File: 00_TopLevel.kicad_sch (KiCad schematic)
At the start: 0 parts

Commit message: Further schematic structure
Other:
- added sheet 01_PowerInput (01_PowerInput.kicad_sch)
- added sheet 02_5VReg (02_5VReg.kicad_sch)
- added sheet 03_CoreReg (03_CoreReg.kicad_sch)
- added sheet 04_USB7206Core (04_USB7206Core.kicad_sch)
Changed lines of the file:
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@@
 	(generator_version "10.0")
 	(paper "A4")
+	(sheet
+		(at 88.9 25.4)
+		(size 38.1 25.4)
+		(exclude_from_sim no)
+		(in_bom yes)
+		(on_board yes)
+		(dnp no)
+		(fields_autoplaced yes)
+		(stroke
+			(width 0.1524)
+			(type solid)
+		)
+		(fill
+			(color 0 0 0 0)
+		)
+		(property "Sheetname" "02_5VReg"
+			(at 88.9 24.6884 0)
+			(show_name no)
+			(do_not_autoplace no)
+			(effects
+				(font
+					(size 1.27 1.27)
+				)
+				(justify left bottom)
+			)
+		)
+		(property "Sheetfile" "02_5VReg.kicad_sch"
+			(at 88.9 51.3846 0)
+			(show_name no)
+			(do_not_autoplace no)
+			(effects
+				(font
+					(size 1.27 1.27)
+				)
+				(justify left top)
+			)
+		)
+		(instances
+			(project "EW.HW.DeskHub1A"
+				(path "/65fce0e0-5101-4e3f-b581-6a8378cbf342/d44490f4-9653-46c1-8023-512c039c6cad"
+					(page "5")
+				)
+			)
+		)
+	)
+	(sheet
+		(at 165.1 25.4)
+		(size 38.1 76.2)
+		(exclude_from_sim no)
+		(in_bom yes)
+		(on_board yes)
+		(dnp no)
+		(fields_autoplaced yes)
+		(stroke
+			(width 0.1524)
+			(type solid)
+		)
+		(fill
+			(color 0 0 0 0)
+		)
+		(property "Sheetname" "04_USB7206Core"
+			(at 165.1 24.6884 0)
+			(show_name no)
+			(do_not_autoplace no)
+			(effects
+				(font
+					(size 1.27 1.27)
+				)
+				(justify left bottom)
+			)
+		)
+		(property "Sheetfile" "04_USB7206Core.kicad_sch"
+			(at 165.1 102.1846 0)
+			(show_name no)
+			(do_not_autoplace no)
+			(effects
+				(font
+					(size 1.27 1.27)
+				)
+				(justify left top)
+			)
+		)
+		(instances
+			(project "EW.HW.DeskHub1A"
+				(path "/65fce0e0-5101-4e3f-b581-6a8378cbf342/d44490f4-9653-46c1-8023-512c039c6cad"
+					(page "4")
+				)
+			)
+		)
+	)
+	(sheet
+		(at 25.4 25.4)
+		(size 38.1 25.4)
+		(exclude_from_sim no)
+		(in_bom yes)
+		(on_board yes)
+		(dnp no)
+		(fields_autoplaced yes)
+		(stroke
+			(width 0.1524)
+			(type solid)
+		)
+		(fill
+			(color 0 0 0 0)
+		)
+		(property "Sheetname" "01_PowerInput"
+			(at 25.4 24.6884 0)
+			(show_name no)
+			(do_not_autoplace no)
+			(effects
+				(font
+					(size 1.27 1.27)
+				)
+				(justify left bottom)
+			)
+		)
+		(property "Sheetfile" "01_PowerInput.kicad_sch"
+			(at 25.4 51.3846 0)
+			(show_name no)
+			(do_not_autoplace no)
+			(effects
+				(font
+					(size 1.27 1.27)
+				)
+				(justify left top)
+			)
+		)
+		(instances
+			(project "EW.HW.DeskHub1A"
+				(path "/65fce0e0-5101-4e3f-b581-6a8378cbf342/d44490f4-9653-46c1-8023-512c039c6cad"
+					(page "3")
+				)
+			)
+		)
+	)
+	(sheet
+		(at 88.9 63.5)
+		(size 38.1 25.4)
+		(exclude_from_sim no)
+		(in_bom yes)
+		(on_board yes)
+		(dnp no)
+		(fields_autoplaced yes)
+		(stroke
+			(width 0.1524)
+			(type solid)
+		)
+		(fill
+			(color 0 0 0 0)
+		)
+		(property "Sheetname" "03_CoreReg"
+			(at 88.9 62.7884 0)
+			(show_name no)
+			(do_not_autoplace no)
+			(effects
+				(font
+					(size 1.27 1.27)
+				)
+				(justify left bottom)
+			)
+		)
+		(property "Sheetfile" "03_CoreReg.kicad_sch"
+			(at 88.9 89.4846 0)
+			(show_name no)
+			(do_not_autoplace no)
+			(effects
+				(font
+					(size 1.27 1.27)
+				)
+				(justify left top)
+			)
+		)
+		(instances
+			(project "EW.HW.DeskHub1A"
+				(path "/65fce0e0-5101-4e3f-b581-6a8378cbf342/d44490f4-9653-46c1-8023-512c039c6cad"
+					(page "6")
+				)
+			)
+		)
+	)
 )

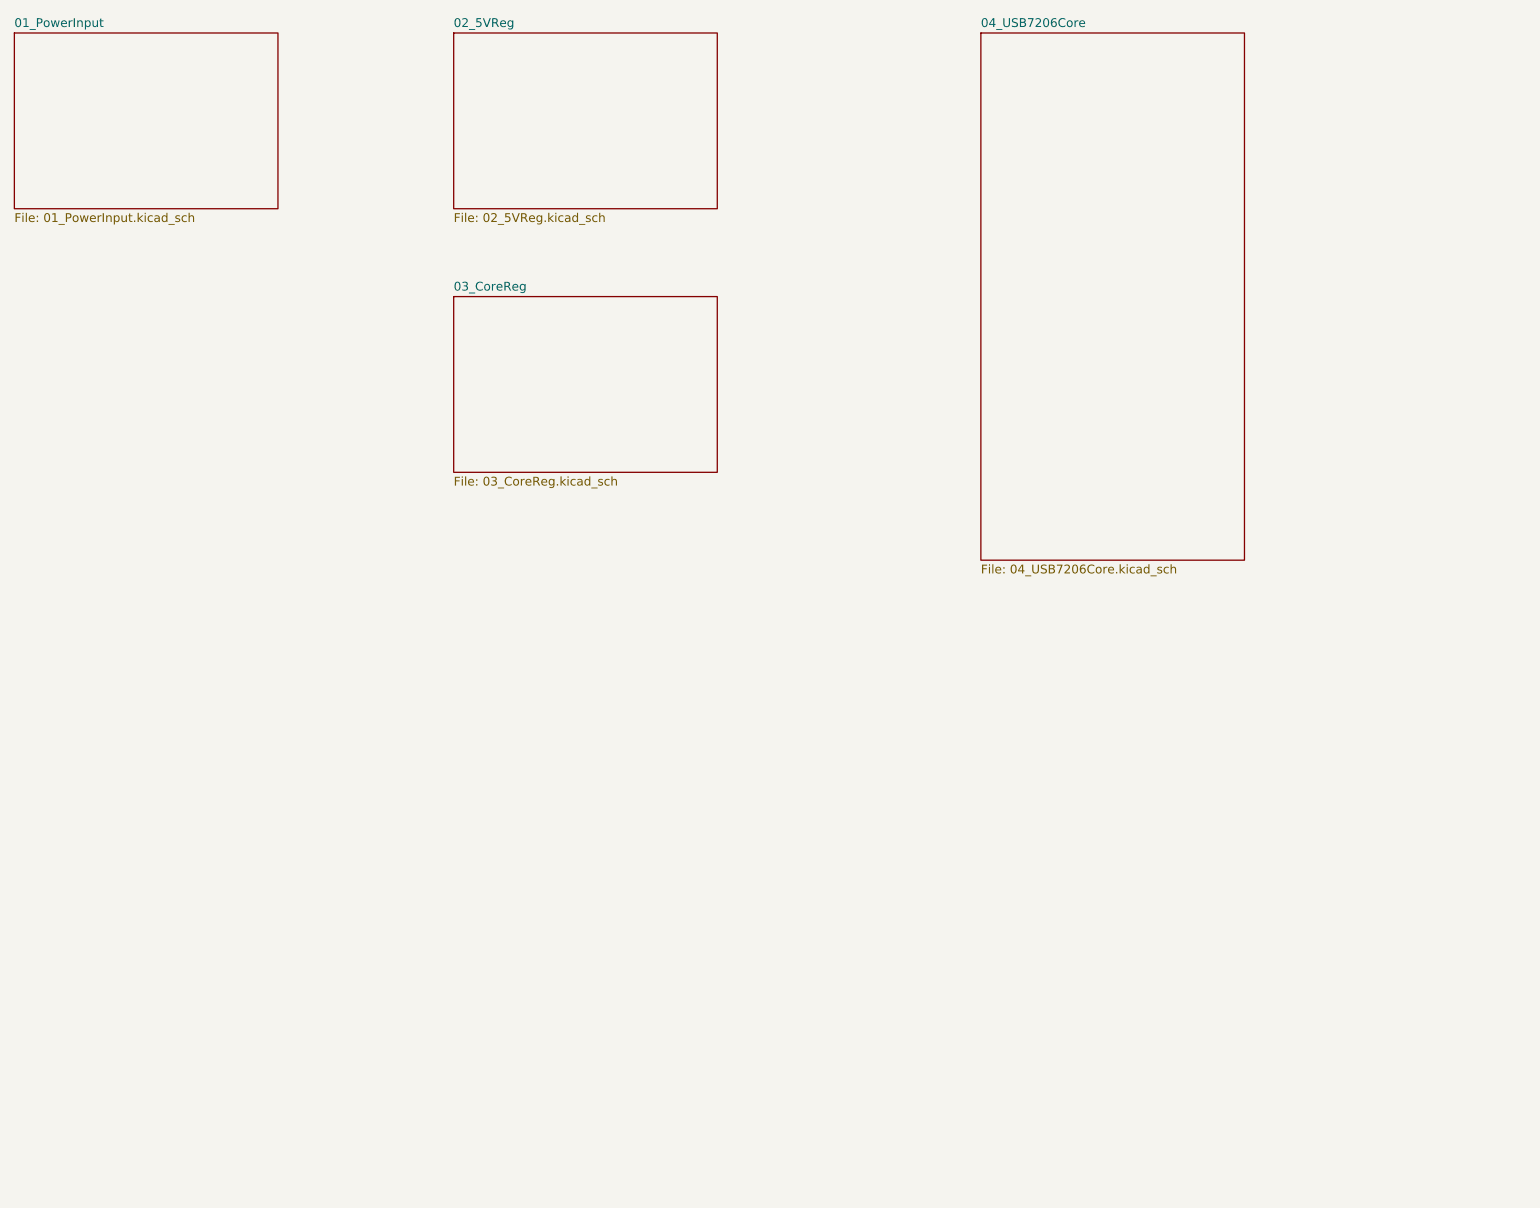
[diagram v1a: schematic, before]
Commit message: Updated sheets to A3, added core IC, power rails, decoupling caps and USB Bus defs
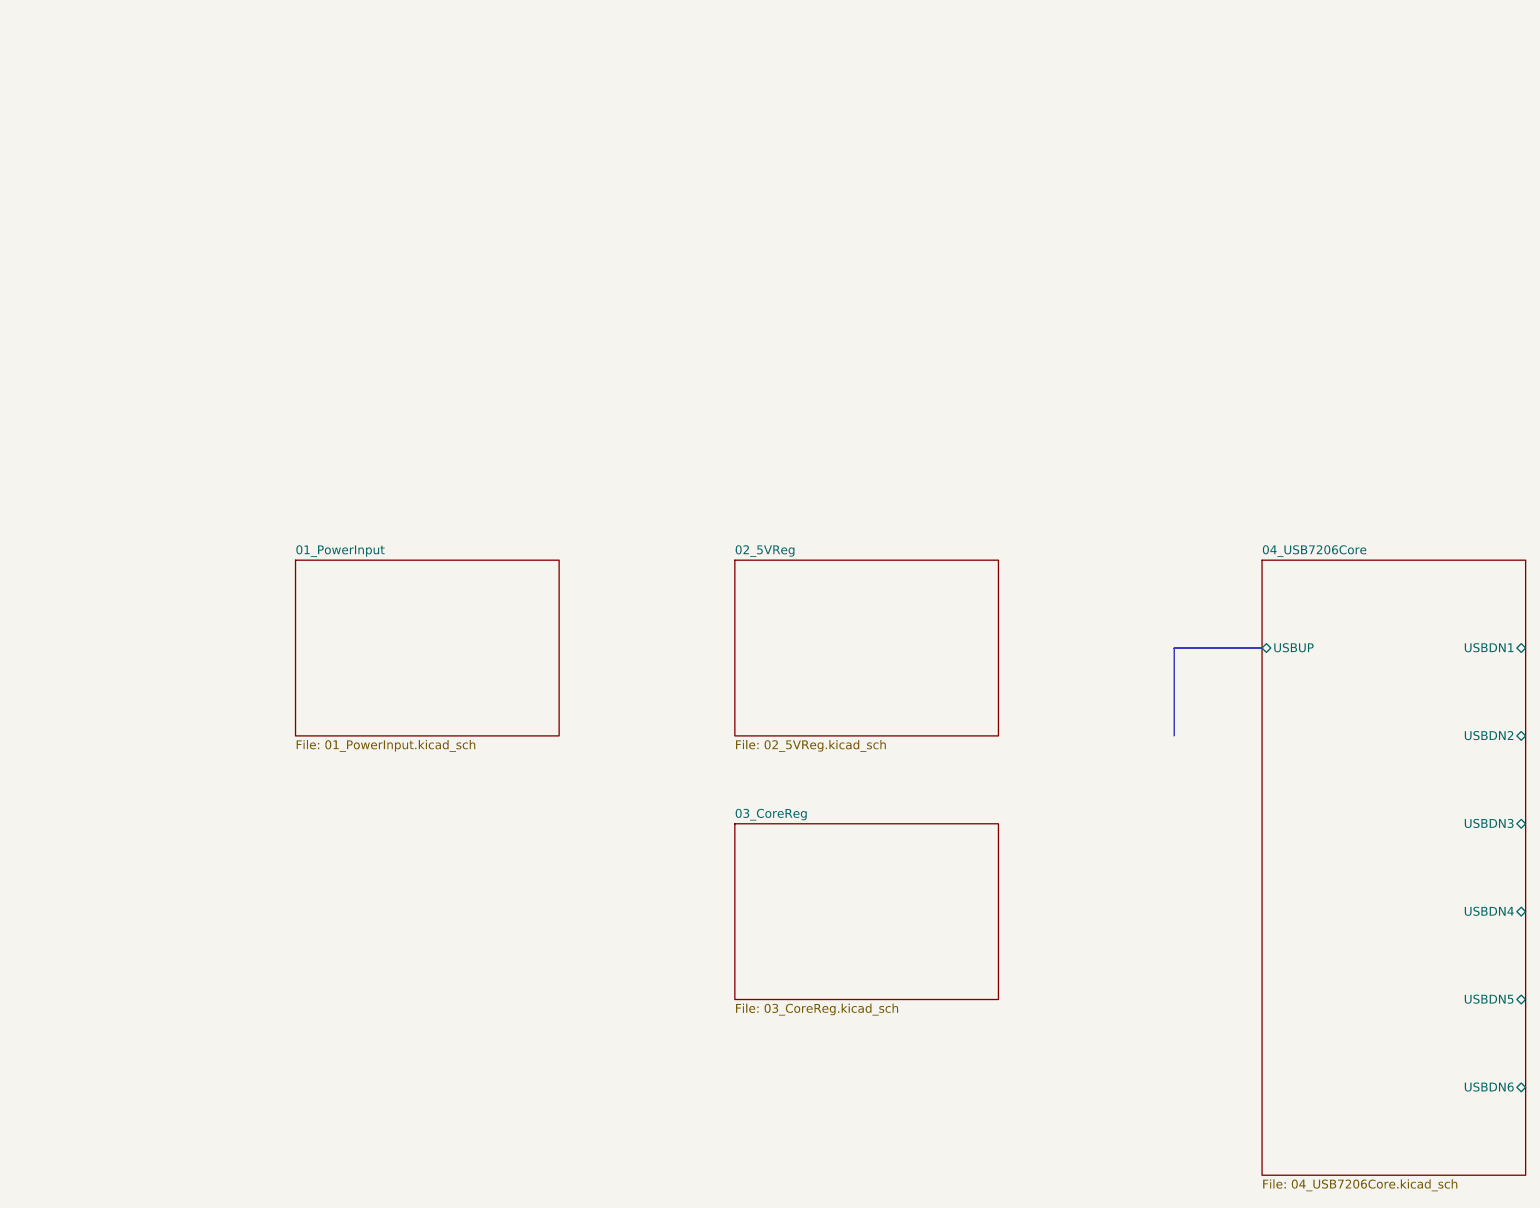
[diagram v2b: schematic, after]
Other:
- sheet 04_USB7206Core ports: added USBDN1, USBDN2, USBDN3, USBDN4, USBDN5, USBDN6, USBUP; removed none
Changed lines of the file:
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@@
 	(generator "eeschema")
 	(generator_version "10.0")
-	(paper "A4")
-	(sheet
-		(at 88.9 25.4)
+	(paper "A3")
+	(bus
+		(pts
+			(xy 193.04 114.3) (xy 193.04 127)
+		)
+		(stroke
+			(width 0)
+			(type default)
+		)
+	)
+	(bus
+		(pts
+			(xy 205.74 114.3) (xy 193.04 114.3)
+		)
+		(stroke
+			(width 0)
+			(type default)
+		)
+	)
+	(sheet
+		(at 129.54 101.6)
 		(size 38.1 25.4)
 		(exclude_from_sim no)
@@
 		)
 		(property "Sheetname" "02_5VReg"
-			(at 88.9 24.6884 0)
+			(at 129.54 100.8884 0)
 			(show_name no)
 			(do_not_autoplace no)
@@
 		)
 		(property "Sheetfile" "02_5VReg.kicad_sch"
-			(at 88.9 51.3846 0)
+			(at 129.54 127.5846 0)
 			(show_name no)
 			(do_not_autoplace no)
@@
 	)
 	(sheet
-		(at 165.1 25.4)
-		(size 38.1 76.2)
+		(at 205.74 101.6)
+		(size 38.1 88.9)
 		(exclude_from_sim no)
 		(in_bom yes)
@@
 		)
 		(property "Sheetname" "04_USB7206Core"
-			(at 165.1 24.6884 0)
+			(at 205.74 100.8884 0)
 			(show_name no)
 			(do_not_autoplace no)
@@
 		)
 		(property "Sheetfile" "04_USB7206Core.kicad_sch"
-			(at 165.1 102.1846 0)
+			(at 205.74 191.0846 0)
 			(show_name no)
 			(do_not_autoplace no)
@@
 				)
 				(justify left top)
+			)
+		)
+		(pin "USBUP" bidirectional
+			(at 205.74 114.3 180)
+			(effects
+				(font
+					(size 1.27 1.27)
+				)
+				(justify left)
+			)
+		)
+		(pin "USBDN3" bidirectional
+			(at 243.84 139.7 0)
+			(effects
+				(font
+					(size 1.27 1.27)
+				)
+				(justify right)
+			)
+		)
+		(pin "USBDN4" bidirectional
+			(at 243.84 152.4 0)
+			(effects
+				(font
+					(size 1.27 1.27)
+				)
+				(justify right)
+			)
+		)
+		(pin "USBDN5" bidirectional
+			(at 243.84 165.1 0)
+			(effects
+				(font
+					(size 1.27 1.27)
+				)
+				(justify right)
+			)
+		)
+		(pin "USBDN1" bidirectional
+			(at 243.84 114.3 0)
+			(effects
+				(font
+					(size 1.27 1.27)
+				)
+				(justify right)
+			)
+		)
+		(pin "USBDN2" bidirectional
+			(at 243.84 127 0)
+			(effects
+				(font
+					(size 1.27 1.27)
+				)
+				(justify right)
+			)
+		)
+		(pin "USBDN6" bidirectional
+			(at 243.84 177.8 0)
+			(effects
+				(font
+					(size 1.27 1.27)
+				)
+				(justify right)
 			)
 		)
@@
 	)
 	(sheet
-		(at 25.4 25.4)
+		(at 66.04 101.6)
 		(size 38.1 25.4)
 		(exclude_from_sim no)
@@
 		)
 		(property "Sheetname" "01_PowerInput"
-			(at 25.4 24.6884 0)
+			(at 66.04 100.8884 0)
 			(show_name no)
 			(do_not_autoplace no)
@@
 		)
 		(property "Sheetfile" "01_PowerInput.kicad_sch"
-			(at 25.4 51.3846 0)
+			(at 66.04 127.5846 0)
 			(show_name no)
 			(do_not_autoplace no)
@@
 	)
 	(sheet
-		(at 88.9 63.5)
+		(at 129.54 139.7)
 		(size 38.1 25.4)
 		(exclude_from_sim no)
@@
 		)
 		(property "Sheetname" "03_CoreReg"
-			(at 88.9 62.7884 0)
+			(at 129.54 138.9884 0)
 			(show_name no)
 			(do_not_autoplace no)
@@
 		)
 		(property "Sheetfile" "03_CoreReg.kicad_sch"
-			(at 88.9 89.4846 0)
-			(show_name no)
-			(do_not_autoplace no)
+			(at 129.54 165.6846 0)
+			(show_name no)
+			(do_not_autoplace no)
